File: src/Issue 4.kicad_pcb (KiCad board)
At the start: 2 copper layers, 213.4 x 130.8 mm, 199 parts, among them IC1 ULA, IC10 4116, IC11 4116, IC12 4116, IC13 4116, IC14 LM1889, IC15 4532, IC16 4532, IC17 4532, IC18 4532, IC19 4532, IC2 Z80, IC20 4532, IC21 4532, IC22 4532, IC23 74LS32, IC24 74LS00, IC25 74LS157, IC26 74LS157, IC3 LS157, IC4 LS157, IC5 ROM, IC6 4116, IC7 4116, IC8 4116, IC9 4116, J1 OKI, J10 UR3, J11 UR4, J2 TI, J3 TI, J4 TI, J7 Barrel_Jack_MountingPin, J8 UR1, J9 UR2, T1 Coil, X1 14Mhz, X2 4.43Mhz

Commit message: 3d model of the coil
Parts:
- IC1, IC2: footprint Package_DIP:DIP-40_W15.24mm -> Package_DIP:DIP-40_W15.24mm_Socket
- IC10, IC11, IC12, IC13, IC15, IC16, IC17, IC18, IC19, IC20, IC21, IC22, IC25, IC26, IC3, IC4, IC6, IC7, IC8, IC9: footprint Package_DIP:DIP-16_W7.62mm -> Package_DIP:DIP-16_W7.62mm_Socket
- IC14: footprint Package_DIP:DIP-18_W7.62mm -> Package_DIP:DIP-18_W7.62mm_Socket
- IC23, IC24: footprint Package_DIP:DIP-14_W7.62mm -> Package_DIP:DIP-14_W7.62mm_Socket
- IC5: footprint Package_DIP:DIP-28_W15.24mm -> Package_DIP:DIP-28_W15.24mm_Socket
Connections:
- C1 pad 1: +5V -> -5V
- C1 pad 2: +5V -> GND
- C2 pad 1: +5V -> -5V
- C2 pad 2: +5V -> GND
- C25 pad 2: +5V -> GND
- C26 pad 2: +5V -> GND
- C27 pad 2: +5V -> GND
- C28 pad 2: +5V -> GND
- C29 pad 1: +5V -> GND
- C3 pad 1: +5V -> -5V
- C3 pad 2: +5V -> GND
- C30 pad 1: +5V -> GND
- C33 pad 1: +5V -> GND
- C34 pad 2: +5V -> GND
- C35 pad 1: +5V -> GND
- C37 pad 2: +5V -> GND
- C4 pad 1: +5V -> -5V
- C4 pad 2: +5V -> GND
- C40 pad 2: +5V -> GND
- C41 pad 2: +5V -> GND
- C42 pad 2: +5V -> GND
- C43 pad 1: +5V -> GND
- C44 pad 2: +5V -> GND
- C45 pad 2: +5V -> GND
- C48 pad 1: +5V -> GND
- C49 pad 1: +5V -> GND
- C5 pad 2: +5V -> GND
- C50 pad 2: +5V -> GND
- C55 pad 1: +5V -> GND
- C56 pad 1: +5V -> GND
- C57 pad 1: +5V -> GND
- C58 pad 1: +5V -> GND
- C59 pad 1: +5V -> GND
- C6 pad 2: +5V -> GND
- C60 pad 1: +5V -> GND
- C62 pad 1: +5V -> GND
- C63 pad 2: +5V -> GND
- C64 pad 1: /_URAS -> Net-(C64-Pad1)
- C64 pad 2: +5V -> GND
- C66 pad 1: +5V -> GND
- C7 pad 2: +5V -> GND
- C72 pad 2: +5V -> GND
- C73 pad 1: +5V -> GND
- C75 pad 1: +5V -> GND
- C76 pad 1: +5V -> GND
- C79 pad 1: +5V -> GND
- C8 pad 2: +5V -> GND
- D11 pad 1: +5V -> GND
- D13 pad 2: +5V -> GND
- D17 pad 2: +5V -> GND
- D19 pad 1: +5V -> GND
- D19 pad 2: +5V -> -5V
- E1 pad 19: +5V -> -5V
- E1 pad 27: unconnected-(E1-Pad27) -> Net-(E1-Pad27)
- E1 pad 32: +5V -> GND
- E1 pad 33: +5V -> GND
- E1 pad 4: unconnected-(E1-Pad4) -> Net-(E1-Pad4)
- E1 pad 40: +5V -> GND
- Ear0 pad 1: +5V -> GND
- IC1 pad 40: +5V -> GND
- IC10 pad 1: +5V -> -5V
- IC10 pad 16: +5V -> GND
- IC11 pad 1: +5V -> -5V
- IC11 pad 16: +5V -> GND
- IC12 pad 1: +5V -> -5V
- IC12 pad 16: +5V -> GND
- IC13 pad 1: +5V -> -5V
- IC13 pad 16: +5V -> GND
- IC14 pad 5: +5V -> GND
- IC15 pad 1: +5V -> GND
- IC15 pad 16: +5V -> GND
- IC16 pad 1: +5V -> GND
- IC16 pad 16: +5V -> GND
- IC17 pad 1: +5V -> GND
- IC17 pad 16: +5V -> GND
- IC18 pad 1: +5V -> GND
- IC18 pad 16: +5V -> GND
- IC19 pad 1: +5V -> GND
- IC19 pad 16: +5V -> GND
- IC2 pad 29: +5V -> GND
- IC20 pad 1: +5V -> GND
- IC20 pad 16: +5V -> GND
- IC21 pad 1: +5V -> GND
- IC21 pad 16: +5V -> GND
- IC22 pad 1: +5V -> GND
- IC22 pad 16: +5V -> GND
- IC23 pad 5: /_URAS -> Net-(C64-Pad1)
- IC23 pad 7: +5V -> GND
- IC24 pad 7: +5V -> GND
- IC25 pad 15: +5V -> GND
- IC25 pad 8: +5V -> GND
- IC26 pad 15: +5V -> GND
- IC26 pad 8: +5V -> GND
- IC3 pad 15: +5V -> GND
- IC3 pad 8: +5V -> GND
- IC4 pad 15: +5V -> GND
- IC4 pad 8: +5V -> GND
- IC5 pad 14: +5V -> GND
- IC6 pad 1: +5V -> -5V
- IC6 pad 16: +5V -> GND
- IC7 pad 1: +5V -> -5V
- IC7 pad 16: +5V -> GND
- IC8 pad 1: +5V -> -5V
- IC8 pad 16: +5V -> GND
- IC9 pad 1: +5V -> -5V
- IC9 pad 16: +5V -> GND
- J3 pad 2: +5V -> GND
- J4 pad 2: +5V -> GND
- J7 pad 1: +5V -> GND
- LS1 pad 1: +5V -> GND
- Mic0 pad 1: +5V -> GND
- R37 pad 2: +5V -> GND
- R43 pad 1: +5V -> GND
- R46 pad 1: +5V -> GND
- R47 pad 1: +5V -> GND
- R50 pad 1: +5V -> GND
- R52 pad 1: +5V -> GND
- R53 pad 1: +5V -> GND
- R56 pad 2: +5V -> GND
- R58 pad 2: +5V -> GND
- R63 pad 2: +5V -> GND
- R70 pad 2: /_URAS -> Net-(C64-Pad1)
- R79 pad 2: +5V -> -5V
- REG1 pad 2: +5V -> GND
- TR3 pad 3: +5V -> GND
- TR4 pad 3: +5V -> GND
- TV1 pad 3: +5V -> GND
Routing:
- net +5V: track 3382.8 -> 1129.1 mm, vias 80 -> 34
- net GND: track 0.00 -> 1856.5 mm, vias 0 -> 36
- net -5V: track 0.00 -> 397.1 mm, vias 0 -> 10
- net Net-(C64-Pad1): track 0.00 -> 107.0 mm, vias 0 -> 5
- net /_URAS: track 245.0 -> 138.0 mm, vias 7 -> 2
- added copper zone on B.Cu, net GND
- added copper zone on F.Cu, net GND
- removed copper zone on B.Cu, net +5V

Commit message: created ibom
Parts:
- IC1, IC2: footprint Package_DIP:DIP-40_W15.24mm_Socket -> Package_DIP:DIP-40_W15.24mm
- IC10, IC11, IC12, IC13, IC15, IC16, IC17, IC18, IC19, IC20, IC21, IC22, IC25, IC26, IC3, IC4, IC6, IC7, IC8, IC9: footprint Package_DIP:DIP-16_W7.62mm_Socket -> Package_DIP:DIP-16_W7.62mm
- IC14: footprint Package_DIP:DIP-18_W7.62mm_Socket -> Package_DIP:DIP-18_W7.62mm
- IC23, IC24: footprint Package_DIP:DIP-14_W7.62mm_Socket -> Package_DIP:DIP-14_W7.62mm
- IC5: footprint Package_DIP:DIP-28_W15.24mm_Socket -> Package_DIP:DIP-28_W15.24mm
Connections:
- C1 pad 1: -5V -> +5V
- C1 pad 2: GND -> +5V
- C2 pad 1: -5V -> +5V
- C2 pad 2: GND -> +5V
- C25 pad 2: GND -> +5V
- C26 pad 2: GND -> +5V
- C27 pad 2: GND -> +5V
- C28 pad 2: GND -> +5V
- C29 pad 1: GND -> +5V
- C3 pad 1: -5V -> +5V
- C3 pad 2: GND -> +5V
- C30 pad 1: GND -> +5V
- C33 pad 1: GND -> +5V
- C34 pad 2: GND -> +5V
- C35 pad 1: GND -> +5V
- C37 pad 2: GND -> +5V
- C4 pad 1: -5V -> +5V
- C4 pad 2: GND -> +5V
- C40 pad 2: GND -> +5V
- C41 pad 2: GND -> +5V
- C42 pad 2: GND -> +5V
- C43 pad 1: GND -> +5V
- C44 pad 2: GND -> +5V
- C45 pad 2: GND -> +5V
- C48 pad 1: GND -> +5V
- C49 pad 1: GND -> +5V
- C5 pad 2: GND -> +5V
- C50 pad 2: GND -> +5V
- C55 pad 1: GND -> +5V
- C56 pad 1: GND -> +5V
- C57 pad 1: GND -> +5V
- C58 pad 1: GND -> +5V
- C59 pad 1: GND -> +5V
- C6 pad 2: GND -> +5V
- C60 pad 1: GND -> +5V
- C62 pad 1: GND -> +5V
- C63 pad 2: GND -> +5V
- C64 pad 1: Net-(C64-Pad1) -> /_URAS
- C64 pad 2: GND -> +5V
- C66 pad 1: GND -> +5V
- C7 pad 2: GND -> +5V
- C72 pad 2: GND -> +5V
- C73 pad 1: GND -> +5V
- C75 pad 1: GND -> +5V
- C76 pad 1: GND -> +5V
- C79 pad 1: GND -> +5V
- C8 pad 2: GND -> +5V
- D11 pad 1: GND -> +5V
- D13 pad 2: GND -> +5V
- D17 pad 2: GND -> +5V
- D19 pad 1: GND -> +5V
- D19 pad 2: -5V -> +5V
- E1 pad 19: -5V -> +5V
- E1 pad 27: Net-(E1-Pad27) -> unconnected-(E1-Pad27)
- E1 pad 32: GND -> +5V
- E1 pad 33: GND -> +5V
- E1 pad 4: Net-(E1-Pad4) -> unconnected-(E1-Pad4)
- E1 pad 40: GND -> +5V
- Ear0 pad 1: GND -> +5V
- IC1 pad 40: GND -> +5V
- IC10 pad 1: -5V -> +5V
- IC10 pad 16: GND -> +5V
- IC11 pad 1: -5V -> +5V
- IC11 pad 16: GND -> +5V
- IC12 pad 1: -5V -> +5V
- IC12 pad 16: GND -> +5V
- IC13 pad 1: -5V -> +5V
- IC13 pad 16: GND -> +5V
- IC14 pad 5: GND -> +5V
- IC15 pad 1: GND -> +5V
- IC15 pad 16: GND -> +5V
- IC16 pad 1: GND -> +5V
- IC16 pad 16: GND -> +5V
- IC17 pad 1: GND -> +5V
- IC17 pad 16: GND -> +5V
- IC18 pad 1: GND -> +5V
- IC18 pad 16: GND -> +5V
- IC19 pad 1: GND -> +5V
- IC19 pad 16: GND -> +5V
- IC2 pad 29: GND -> +5V
- IC20 pad 1: GND -> +5V
- IC20 pad 16: GND -> +5V
- IC21 pad 1: GND -> +5V
- IC21 pad 16: GND -> +5V
- IC22 pad 1: GND -> +5V
- IC22 pad 16: GND -> +5V
- IC23 pad 5: Net-(C64-Pad1) -> /_URAS
- IC23 pad 7: GND -> +5V
- IC24 pad 7: GND -> +5V
- IC25 pad 15: GND -> +5V
- IC25 pad 8: GND -> +5V
- IC26 pad 15: GND -> +5V
- IC26 pad 8: GND -> +5V
- IC3 pad 15: GND -> +5V
- IC3 pad 8: GND -> +5V
- IC4 pad 15: GND -> +5V
- IC4 pad 8: GND -> +5V
- IC5 pad 14: GND -> +5V
- IC6 pad 1: -5V -> +5V
- IC6 pad 16: GND -> +5V
- IC7 pad 1: -5V -> +5V
- IC7 pad 16: GND -> +5V
- IC8 pad 1: -5V -> +5V
- IC8 pad 16: GND -> +5V
- IC9 pad 1: -5V -> +5V
- IC9 pad 16: GND -> +5V
- J3 pad 2: GND -> +5V
- J4 pad 2: GND -> +5V
- J7 pad 1: GND -> +5V
- LS1 pad 1: GND -> +5V
- Mic0 pad 1: GND -> +5V
- R37 pad 2: GND -> +5V
- R43 pad 1: GND -> +5V
- R46 pad 1: GND -> +5V
- R47 pad 1: GND -> +5V
- R50 pad 1: GND -> +5V
- R52 pad 1: GND -> +5V
- R53 pad 1: GND -> +5V
- R56 pad 2: GND -> +5V
- R58 pad 2: GND -> +5V
- R63 pad 2: GND -> +5V
- R70 pad 2: Net-(C64-Pad1) -> /_URAS
- R79 pad 2: -5V -> +5V
- REG1 pad 2: GND -> +5V
- TR3 pad 3: GND -> +5V
- TR4 pad 3: GND -> +5V
- TV1 pad 3: GND -> +5V
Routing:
- net +5V: track 1129.1 -> 3442.3 mm, vias 34 -> 81
- net GND: track 1856.5 -> 0.00 mm, vias 36 -> 0
- net -5V: track 397.1 -> 0.00 mm, vias 10 -> 0
- net Net-(C64-Pad1): track 107.0 -> 0.00 mm, vias 5 -> 0
- net /_URAS: track 138.0 -> 245.0 mm, vias 2 -> 7
- net Net-(T1-AB): track 59.7 -> 0.00 mm, vias 1 -> 0
- net Net-(T1-AA): track 41.5 -> 0.00 mm, vias 1 -> 0
- net (no net): track 0.00 -> 41.5 mm, vias 1 -> 2
- added copper zone on B.Cu, net +5V
- removed copper zone on B.Cu, net GND
- removed copper zone on F.Cu, net GND

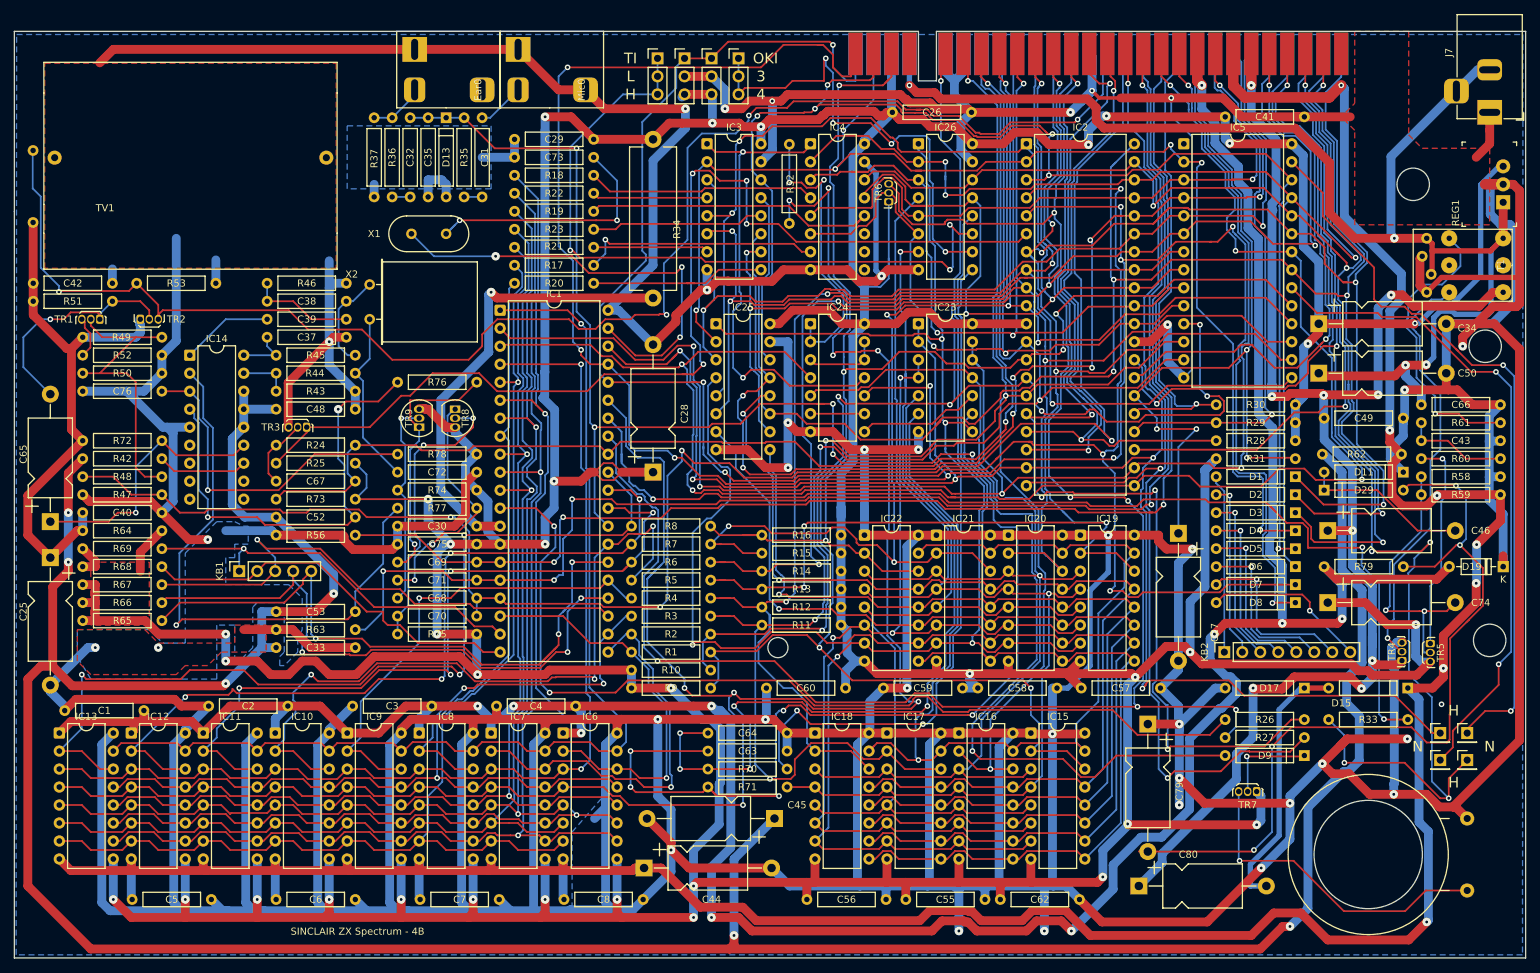
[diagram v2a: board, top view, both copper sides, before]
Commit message: re routed ear and mic and coil
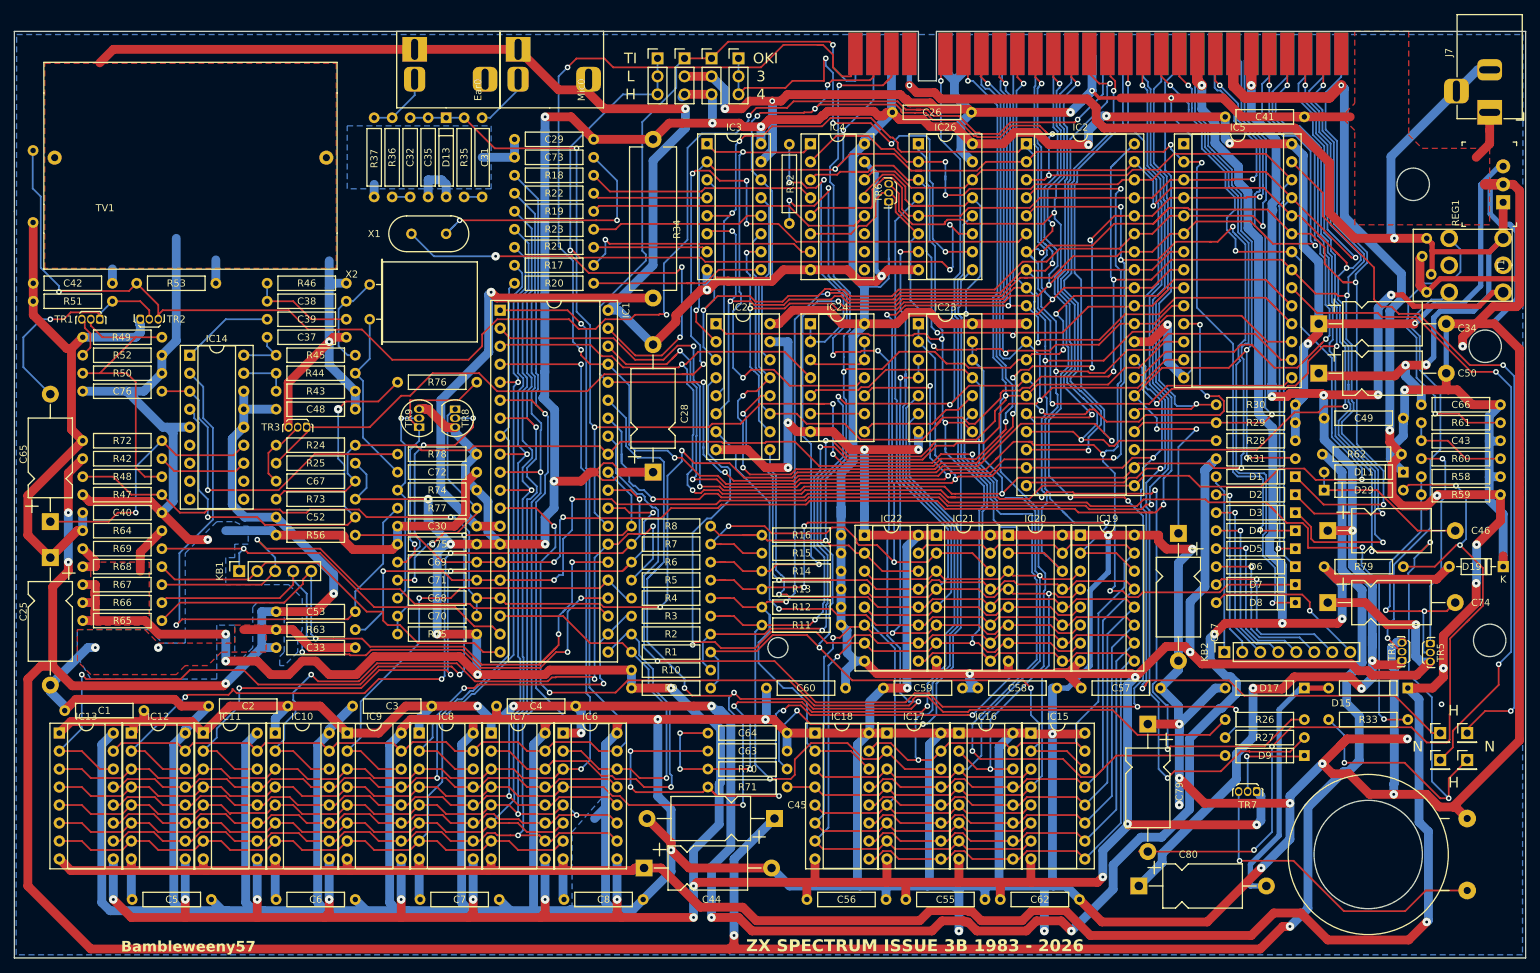
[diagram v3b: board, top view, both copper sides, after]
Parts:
- IC1, IC2: footprint Package_DIP:DIP-40_W15.24mm -> Package_DIP:DIP-40_W15.24mm_Socket
- IC10, IC11, IC12, IC13, IC15, IC16, IC17, IC18, IC19, IC20, IC21, IC22, IC25, IC26, IC3, IC4, IC6, IC7, IC8, IC9: footprint Package_DIP:DIP-16_W7.62mm -> Package_DIP:DIP-16_W7.62mm_Socket
- IC14: footprint Package_DIP:DIP-18_W7.62mm -> Package_DIP:DIP-18_W7.62mm_Socket
- IC23, IC24: footprint Package_DIP:DIP-14_W7.62mm -> Package_DIP:DIP-14_W7.62mm_Socket
- IC5: footprint Package_DIP:DIP-28_W15.24mm -> Package_DIP:DIP-28_W15.24mm_Socket
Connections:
- C1 pad 1: +5V -> -5V
- C1 pad 2: +5V -> GND
- C2 pad 1: +5V -> -5V
- C2 pad 2: +5V -> GND
- C25 pad 2: +5V -> GND
- C26 pad 2: +5V -> GND
- C27 pad 2: +5V -> GND
- C28 pad 2: +5V -> GND
- C29 pad 1: +5V -> GND
- C3 pad 1: +5V -> -5V
- C3 pad 2: +5V -> GND
- C30 pad 1: +5V -> GND
- C33 pad 1: +5V -> GND
- C34 pad 2: +5V -> GND
- C35 pad 1: +5V -> GND
- C37 pad 2: +5V -> GND
- C4 pad 1: +5V -> -5V
- C4 pad 2: +5V -> GND
- C40 pad 2: +5V -> GND
- C41 pad 2: +5V -> GND
- C42 pad 2: +5V -> GND
- C43 pad 1: +5V -> GND
- C44 pad 2: +5V -> GND
- C45 pad 2: +5V -> GND
- C48 pad 1: +5V -> GND
- C49 pad 1: +5V -> GND
- C5 pad 2: +5V -> GND
- C50 pad 2: +5V -> GND
- C55 pad 1: +5V -> GND
- C56 pad 1: +5V -> GND
- C57 pad 1: +5V -> GND
- C58 pad 1: +5V -> GND
- C59 pad 1: +5V -> GND
- C6 pad 2: +5V -> GND
- C60 pad 1: +5V -> GND
- C62 pad 1: +5V -> GND
- C63 pad 2: +5V -> GND
- C64 pad 1: /_URAS -> Net-(C64-Pad1)
- C64 pad 2: +5V -> GND
- C66 pad 1: +5V -> GND
- C7 pad 2: +5V -> GND
- C72 pad 2: +5V -> GND
- C73 pad 1: +5V -> GND
- C75 pad 1: +5V -> GND
- C76 pad 1: +5V -> GND
- C79 pad 1: +5V -> GND
- C8 pad 2: +5V -> GND
- D11 pad 1: +5V -> GND
- D13 pad 2: +5V -> GND
- D17 pad 2: +5V -> GND
- D19 pad 1: +5V -> GND
- D19 pad 2: +5V -> -5V
- E1 pad 19: +5V -> -5V
- E1 pad 27: unconnected-(E1-Pad27) -> Net-(E1-Pad27)
- E1 pad 32: +5V -> GND
- E1 pad 33: +5V -> GND
- E1 pad 4: unconnected-(E1-Pad4) -> Net-(E1-Pad4)
- E1 pad 40: +5V -> GND
- Ear0 pad 1: +5V -> GND
- Ear0 pad MP: (no net) -> GND
- IC1 pad 40: +5V -> GND
- IC10 pad 1: +5V -> -5V
- IC10 pad 16: +5V -> GND
- IC11 pad 1: +5V -> -5V
- IC11 pad 16: +5V -> GND
- IC12 pad 1: +5V -> -5V
- IC12 pad 16: +5V -> GND
- IC13 pad 1: +5V -> -5V
- IC13 pad 16: +5V -> GND
- IC14 pad 5: +5V -> GND
- IC15 pad 1: +5V -> GND
- IC15 pad 16: +5V -> GND
- IC16 pad 1: +5V -> GND
- IC16 pad 16: +5V -> GND
- IC17 pad 1: +5V -> GND
- IC17 pad 16: +5V -> GND
- IC18 pad 1: +5V -> GND
- IC18 pad 16: +5V -> GND
- IC19 pad 1: +5V -> GND
- IC19 pad 16: +5V -> GND
- IC2 pad 29: +5V -> GND
- IC20 pad 1: +5V -> GND
- IC20 pad 16: +5V -> GND
- IC21 pad 1: +5V -> GND
- IC21 pad 16: +5V -> GND
- IC22 pad 1: +5V -> GND
- IC22 pad 16: +5V -> GND
- IC23 pad 5: /_URAS -> Net-(C64-Pad1)
- IC23 pad 7: +5V -> GND
- IC24 pad 7: +5V -> GND
- IC25 pad 15: +5V -> GND
- IC25 pad 8: +5V -> GND
- IC26 pad 15: +5V -> GND
- IC26 pad 8: +5V -> GND
- IC3 pad 15: +5V -> GND
- IC3 pad 8: +5V -> GND
- IC4 pad 15: +5V -> GND
- IC4 pad 8: +5V -> GND
- IC5 pad 14: +5V -> GND
- IC6 pad 1: +5V -> -5V
- IC6 pad 16: +5V -> GND
- IC7 pad 1: +5V -> -5V
- IC7 pad 16: +5V -> GND
- IC8 pad 1: +5V -> -5V
- IC8 pad 16: +5V -> GND
- IC9 pad 1: +5V -> -5V
- IC9 pad 16: +5V -> GND
- J3 pad 2: +5V -> GND
- J4 pad 2: +5V -> GND
- J7 pad 1: +5V -> GND
- LS1 pad 1: +5V -> GND
- Mic0 pad 1: +5V -> GND
- Mic0 pad MP: (no net) -> GND
- R37 pad 2: +5V -> GND
- R43 pad 1: +5V -> GND
- R46 pad 1: +5V -> GND
- R47 pad 1: +5V -> GND
- R50 pad 1: +5V -> GND
- R52 pad 1: +5V -> GND
- R53 pad 1: +5V -> GND
- R56 pad 2: +5V -> GND
- R58 pad 2: +5V -> GND
- R63 pad 2: +5V -> GND
- R70 pad 2: /_URAS -> Net-(C64-Pad1)
- R79 pad 2: +5V -> -5V
- REG1 pad 2: +5V -> GND
- T1 pad 7: (no net) -> GND
- TR3 pad 3: +5V -> GND
- TR4 pad 3: +5V -> GND
- TV1 pad 3: +5V -> GND
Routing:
- net +5V: track 3442.3 -> 1129.9 mm, vias 81 -> 34
- net GND: track 0.00 -> 1856.5 mm, vias 0 -> 36
- net -5V: track 0.00 -> 397.1 mm, vias 0 -> 10
- net Net-(C64-Pad1): track 0.00 -> 107.0 mm, vias 0 -> 5
- net /_URAS: track 245.0 -> 138.0 mm, vias 7 -> 2
- net Net-(T1-Pad2): track 0.00 -> 59.7 mm, vias 0 -> 1
- net Net-(R61-Pad2): track 0.00 -> 42.0 mm, vias 0 -> 1
- net (no net): track 41.5 -> 0.00 mm, vias 2 -> 1
- net +9V: track 193.1 -> 191.3 mm
- net A15: track 335.9 -> 336.9 mm
- added copper zone on B.Cu, net GND
- added copper zone on F.Cu, net GND
- removed copper zone on B.Cu, net +5V
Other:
- board text added: "Bambleweeny57"
- board text added: "ZX SPECTRUM ISSUE 3B 1983 - 2026"
- board text removed: "SINCLAIR ZX Spectrum - 4B"
